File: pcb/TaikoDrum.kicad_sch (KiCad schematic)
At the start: 23 parts, among them J1 USB_B_Micro, J2 Conn_02x04_Odd_Even, U1 STM32F103C8Tx, U2 LM3940IMPX-3.3_NOPB, Y1 8Mhz

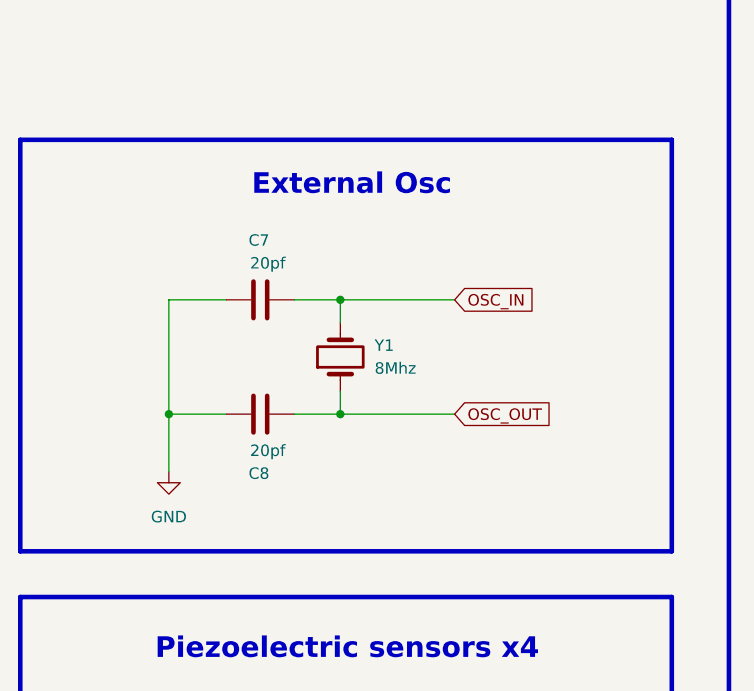
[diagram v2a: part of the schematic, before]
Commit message: Added 16M resistor for external LSE oscillator according to the STM32F103 errata recomendations.
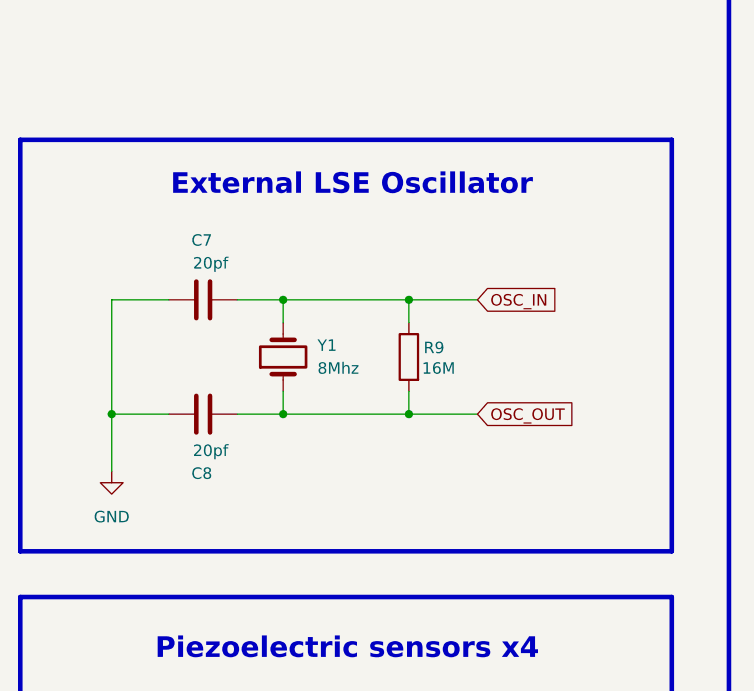
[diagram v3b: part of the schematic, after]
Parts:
- added R9: 16M, Resistor_SMD:R_0805_2012Metric, symbol Device:R
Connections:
- net OSC_IN: now also R9.1
- net OSC_OUT: now also R9.2
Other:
- note added: "External LSE Oscillator"
- note removed: "External Osc"
- moved on the sheet: C7, C8, Y1
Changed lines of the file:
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@@
 		)
 	)
-	(text "External Osc"
+	(text "External LSE Oscillator"
 		(exclude_from_sim no)
 		(at 60.96 43.18 0)
@@
 	)
 	(junction
-		(at 40.64 68.58)
+		(at 34.29 68.58)
 		(diameter 0)
 		(color 0 0 0 0)
@@
 	)
 	(junction
-		(at 59.69 55.88)
+		(at 53.34 55.88)
 		(diameter 0)
 		(color 0 0 0 0)
@@
 	)
 	(junction
-		(at 59.69 68.58)
+		(at 53.34 68.58)
 		(diameter 0)
 		(color 0 0 0 0)
@@
 	)
 	(junction
+		(at 67.31 55.88)
+		(diameter 0)
+		(color 0 0 0 0)
+	)
+	(junction
+		(at 67.31 68.58)
+		(diameter 0)
+		(color 0 0 0 0)
+	)
+	(junction
 		(at 49.53 127)
 		(diameter 0)
@@
 	(wire
 		(pts
-			(xy 40.64 68.58) (xy 40.64 55.88)
+			(xy 34.29 68.58) (xy 34.29 55.88)
 		)
 		(stroke
@@
 	(wire
 		(pts
-			(xy 54.61 68.58) (xy 59.69 68.58)
+			(xy 48.26 68.58) (xy 53.34 68.58)
+		)
+		(stroke
+			(width 0)
+			(type default)
+		)
+	)
+	(wire
+		(pts
+			(xy 53.34 55.88) (xy 67.31 55.88)
 		)
 		(stroke
@@
 	(wire
 		(pts
+			(xy 67.31 66.04) (xy 67.31 68.58)
+		)
+		(stroke
+			(width 0)
+			(type default)
+		)
+	)
+	(wire
+		(pts
 			(xy 55.88 115.57) (xy 76.2 115.57)
 		)
@@
 	(wire
 		(pts
-			(xy 40.64 55.88) (xy 46.99 55.88)
+			(xy 34.29 55.88) (xy 40.64 55.88)
 		)
 		(stroke
@@
 	(wire
 		(pts
+			(xy 67.31 55.88) (xy 67.31 58.42)
+		)
+		(stroke
+			(width 0)
+			(type default)
+		)
+	)
+	(wire
+		(pts
 			(xy 139.7 128.27) (xy 138.43 128.27)
 		)
@@
 	(wire
 		(pts
-			(xy 59.69 68.58) (xy 59.69 66.04)
+			(xy 53.34 68.58) (xy 53.34 66.04)
 		)
 		(stroke
@@
 	(wire
 		(pts
-			(xy 72.39 55.88) (xy 59.69 55.88)
+			(xy 74.93 55.88) (xy 67.31 55.88)
 		)
 		(stroke
@@
 	(wire
 		(pts
-			(xy 40.64 74.93) (xy 40.64 68.58)
+			(xy 34.29 74.93) (xy 34.29 68.58)
 		)
 		(stroke
@@
 	(wire
 		(pts
-			(xy 59.69 58.42) (xy 59.69 55.88)
+			(xy 53.34 58.42) (xy 53.34 55.88)
 		)
 		(stroke
@@
 	(wire
 		(pts
-			(xy 40.64 68.58) (xy 46.99 68.58)
+			(xy 34.29 68.58) (xy 40.64 68.58)
 		)
 		(stroke
@@
 	(wire
 		(pts
-			(xy 72.39 68.58) (xy 59.69 68.58)
+			(xy 74.93 68.58) (xy 67.31 68.58)
 		)
 		(stroke
@@
 	(wire
 		(pts
+			(xy 53.34 68.58) (xy 67.31 68.58)
+		)
+		(stroke
+			(width 0)
+			(type default)
+		)
+	)
+	(wire
+		(pts
 			(xy 57.15 107.95) (xy 80.01 107.95)
 		)
@@
 	(wire
 		(pts
-			(xy 59.69 55.88) (xy 54.61 55.88)
+			(xy 53.34 55.88) (xy 48.26 55.88)
 		)
 		(stroke
@@
 	(global_label "OSC_OUT"
 		(shape input)
-		(at 72.39 68.58 0)
+		(at 74.93 68.58 0)
 		(fields_autoplaced yes)
 		(effects
@@
 		)
 		(property "Intersheetrefs" "${INTERSHEET_REFS}"
-			(at 83.7814 68.58 0)
+			(at 86.3214 68.58 0)
 			(effects
 				(font
@@
 	(global_label "OSC_IN"
 		(shape input)
-		(at 72.39 55.88 0)
+		(at 74.93 55.88 0)
 		(fields_autoplaced yes)
 		(effects
@@
 		)
 		(property "Intersheetrefs" "${INTERSHEET_REFS}"
-			(at 82.0881 55.88 0)
+			(at 84.6281 55.88 0)
 			(effects
 				(font
@@
 	(symbol
 		(lib_id "Device:Crystal")
-		(at 59.69 62.23 90)
+		(at 53.34 62.23 90)
 		(unit 1)
 		(exclude_from_sim no)
@@
 		(fields_autoplaced yes)
 		(property "Reference" "Y1"
-			(at 63.5 60.9599 90)
+			(at 57.15 60.9599 90)
 			(effects
 				(font
@@
 		)
 		(property "Value" "8Mhz"
-			(at 63.5 63.4999 90)
+			(at 57.15 63.4999 90)
 			(effects
 				(font
@@
 		)
 		(property "Footprint" ""
-			(at 59.69 62.23 0)
+			(at 53.34 62.23 0)
 			(effects
 				(font
@@
 		)
 		(property "Datasheet" "~"
-			(at 59.69 62.23 0)
+			(at 53.34 62.23 0)
 			(effects
 				(font
@@
 		)
 		(property "Description" "Two pin crystal"
-			(at 59.69 62.23 0)
+			(at 53.34 62.23 0)
 			(effects
 				(font
@@
 	(symbol
 		(lib_id "Device:C")
-		(at 50.8 55.88 90)
+		(at 44.45 55.88 90)
 		(unit 1)
 		(exclude_from_sim no)
@@
 		(dnp no)
 		(property "Reference" "C7"
-			(at 51.816 49.276 90)
+			(at 45.466 49.276 90)
 			(effects
 				(font
@@
 		)
 		(property "Value" "20pf"
-			(at 53.594 51.816 90)
+			(at 47.244 51.816 90)
 			(effects
 				(font
@@
 		)
 		(property "Footprint" "Capacitor_SMD:C_0805_2012Metric_Pad1.18x1.45mm_HandSolder"
-			(at 54.61 54.9148 0)
+			(at 48.26 54.9148 0)
 			(effects
 				(font
@@
 		)
 		(property "Datasheet" "~"
-			(at 50.8 55.88 0)
+			(at 44.45 55.88 0)
 			(effects
 				(font
@@
 		)
 		(property "Description" "Unpolarized capacitor"
-			(at 50.8 55.88 0)
+			(at 44.45 55.88 0)
 			(effects
 				(font
@@
 	(symbol
 		(lib_id "Device:C")
-		(at 50.8 68.58 90)
+		(at 44.45 68.58 90)
 		(mirror x)
 		(unit 1)
@@
 		(dnp no)
 		(property "Reference" "C8"
-			(at 51.816 75.184 90)
+			(at 45.466 75.184 90)
 			(effects
 				(font
@@
 		)
 		(property "Value" "20pf"
-			(at 53.594 72.644 90)
+			(at 47.244 72.644 90)
 			(effects
 				(font
@@
 		)
 		(property "Footprint" "Capacitor_SMD:C_0805_2012Metric_Pad1.18x1.45mm_HandSolder"
-			(at 54.61 69.5452 0)
+			(at 48.26 69.5452 0)
 			(effects
 				(font
@@
 		)
 		(property "Datasheet" "~"
-			(at 50.8 68.58 0)
+			(at 44.45 68.58 0)
 			(effects
 				(font
@@
 		)
 		(property "Description" "Unpolarized capacitor"
-			(at 50.8 68.58 0)
+			(at 44.45 68.58 0)
 			(effects
 				(font
@@
 	)
 	(symbol
+		(lib_id "Device:R")
+		(at 67.31 62.23 0)
+		(mirror y)
+		(unit 1)
+		(exclude_from_sim no)
+		(in_bom yes)
+		(on_board yes)
+		(dnp no)
+		(property "Reference" "R9"
+			(at 70.104 61.214 0)
+			(effects
+				(font
+					(size 1.27 1.27)
+				)
+			)
+		)
+		(property "Value" "16M"
+			(at 70.612 63.5 0)
+			(effects
+				(font
+					(size 1.27 1.27)
+				)
+			)
+		)
+		(property "Footprint" "Resistor_SMD:R_0805_2012Metric"
+			(at 69.088 62.23 90)
+			(effects
+				(font
+					(size 1.27 1.27)
+				)
+				(hide yes)
+			)
+		)
+		(property "Datasheet" "~"
+			(at 67.31 62.23 0)
+			(effects
+				(font
+					(size 1.27 1.27)
+				)
+				(hide yes)
+			)
+		)
+		(property "Description" "Resistor"
+			(at 67.31 62.23 0)
+			(effects
+				(font
+					(size 1.27 1.27)
+				)
+				(hide yes)
+			)
+		)
+		(pin "1"
+		)
+		(pin "2"
+		)
+		(instances
+			(project "TaikoDrum"
+				(path "/ee4ada02-05a0-4e49-92f9-f61a706c8588"
+					(reference "R9")
+					(unit 1)
+				)
+			)
+		)
+	)
+	(symbol
 		(lib_id "Switch:SW_SPST")
 		(at 36.83 172.72 90)
@@
 	(symbol
 		(lib_id "power:GND")
-		(at 40.64 74.93 0)
+		(at 34.29 74.93 0)
 		(unit 1)
 		(exclude_from_sim no)
@@
 		(fields_autoplaced yes)
 		(property "Reference" "#PWR019"
-			(at 40.64 81.28 0)
+			(at 34.29 81.28 0)
 			(effects
 				(font
@@
 		)
 		(property "Value" "GND"
-			(at 40.64 80.01 0)
+			(at 34.29 80.01 0)
 			(effects
 				(font
@@
 		)
 		(property "Footprint" ""
-			(at 40.64 74.93 0)
+			(at 34.29 74.93 0)
 			(effects
 				(font
@@
 		)
 		(property "Datasheet" ""
-			(at 40.64 74.93 0)
+			(at 34.29 74.93 0)
 			(effects
 				(font
@@
 		)
 		(property "Description" "Power symbol creates a global label with name \"GND\" , ground"
-			(at 40.64 74.93 0)
+			(at 34.29 74.93 0)
 			(effects
 				(font

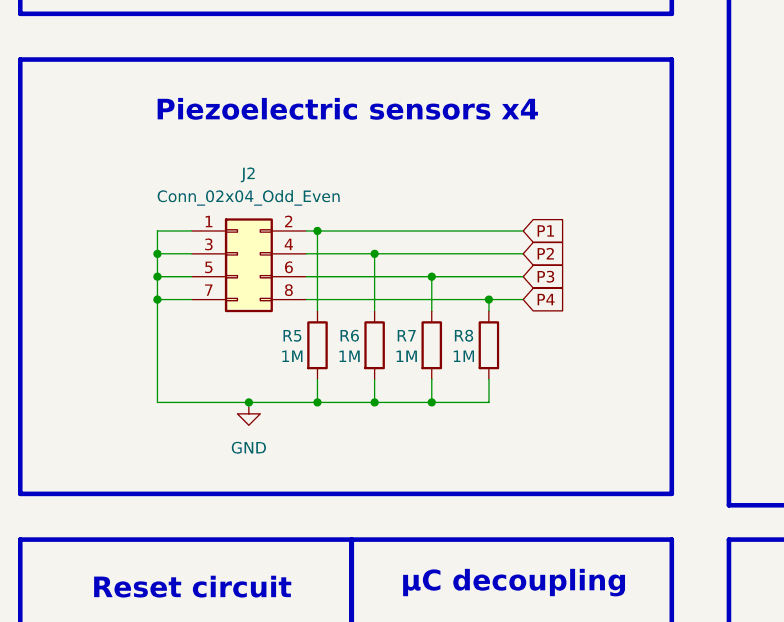
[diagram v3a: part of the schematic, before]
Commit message: Used an additional voltage divider to not loose any energy from the piezo signal.
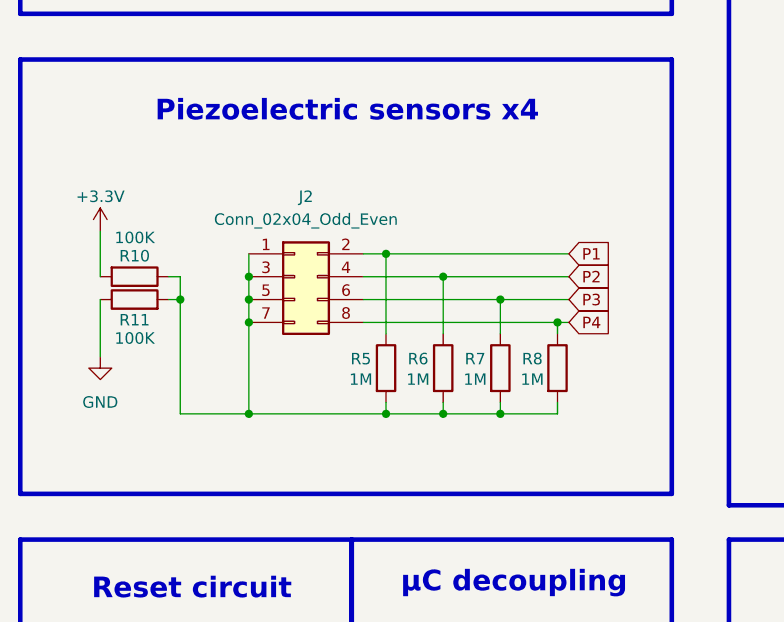
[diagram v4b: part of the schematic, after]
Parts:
- added R10, R11: 100K, Resistor_SMD:R_0805_2012Metric, symbol Device:R
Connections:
- net +3.3V: now also R10.2
- net GND: now also R11.1; no longer J2.1 (Pin_1), J2.3 (Pin_3), J2.5 (Pin_5), J2.7 (Pin_7), R5.2, R6.2, R7.2, R8.2
- new net: J2.1 (Pin_1), J2.3 (Pin_3), J2.5 (Pin_5), J2.7 (Pin_7), R10.1, R11.2, R5.2, R6.2, R7.2, R8.2
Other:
- moved on the sheet: J2, R5, R6, R7, R8

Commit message: Updated PCB schematic.
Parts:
- added D1: PWR, LED_THT:LED_D3.0mm, symbol Device:LED
- added H1, H2, H3, H4: MountingHole, MountingHole:MountingHole_2.2mm_M2, symbol Mechanical:MountingHole
- added R12: 1K, Resistor_THT:R_Axial_DIN0204_L3.6mm_D1.6mm_P2.54mm_Vertical, symbol Device:R
- C3, C4, C5, C6, C7, C8: footprint Capacitor_SMD:C_0805_2012Metric_Pad1.18x1.45mm_HandSolder -> Capacitor_THT:C_Radial_D5.0mm_H5.0mm_P2.00mm
- R1, R10, R11, R2, R3, R4, R5, R6, R7, R8, R9: footprint Resistor_SMD:R_0805_2012Metric -> Resistor_THT:R_Axial_DIN0204_L3.6mm_D1.6mm_P2.54mm_Vertical
- Y1: footprint (none) -> Crystal:Crystal_HC52-U_Vertical
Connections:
- net +3.3V: now also R12.2
- net GND: now also D1.1 (K)
- new net: D1.2 (A), R12.1
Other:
- note added: "Miscs"
- note removed: "Reset circuit"
- note removed: "µC decoupling"
- moved on the sheet: C1, C2, C3, C4, C5, C6, C7, C8, J1, J2, R1, R10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

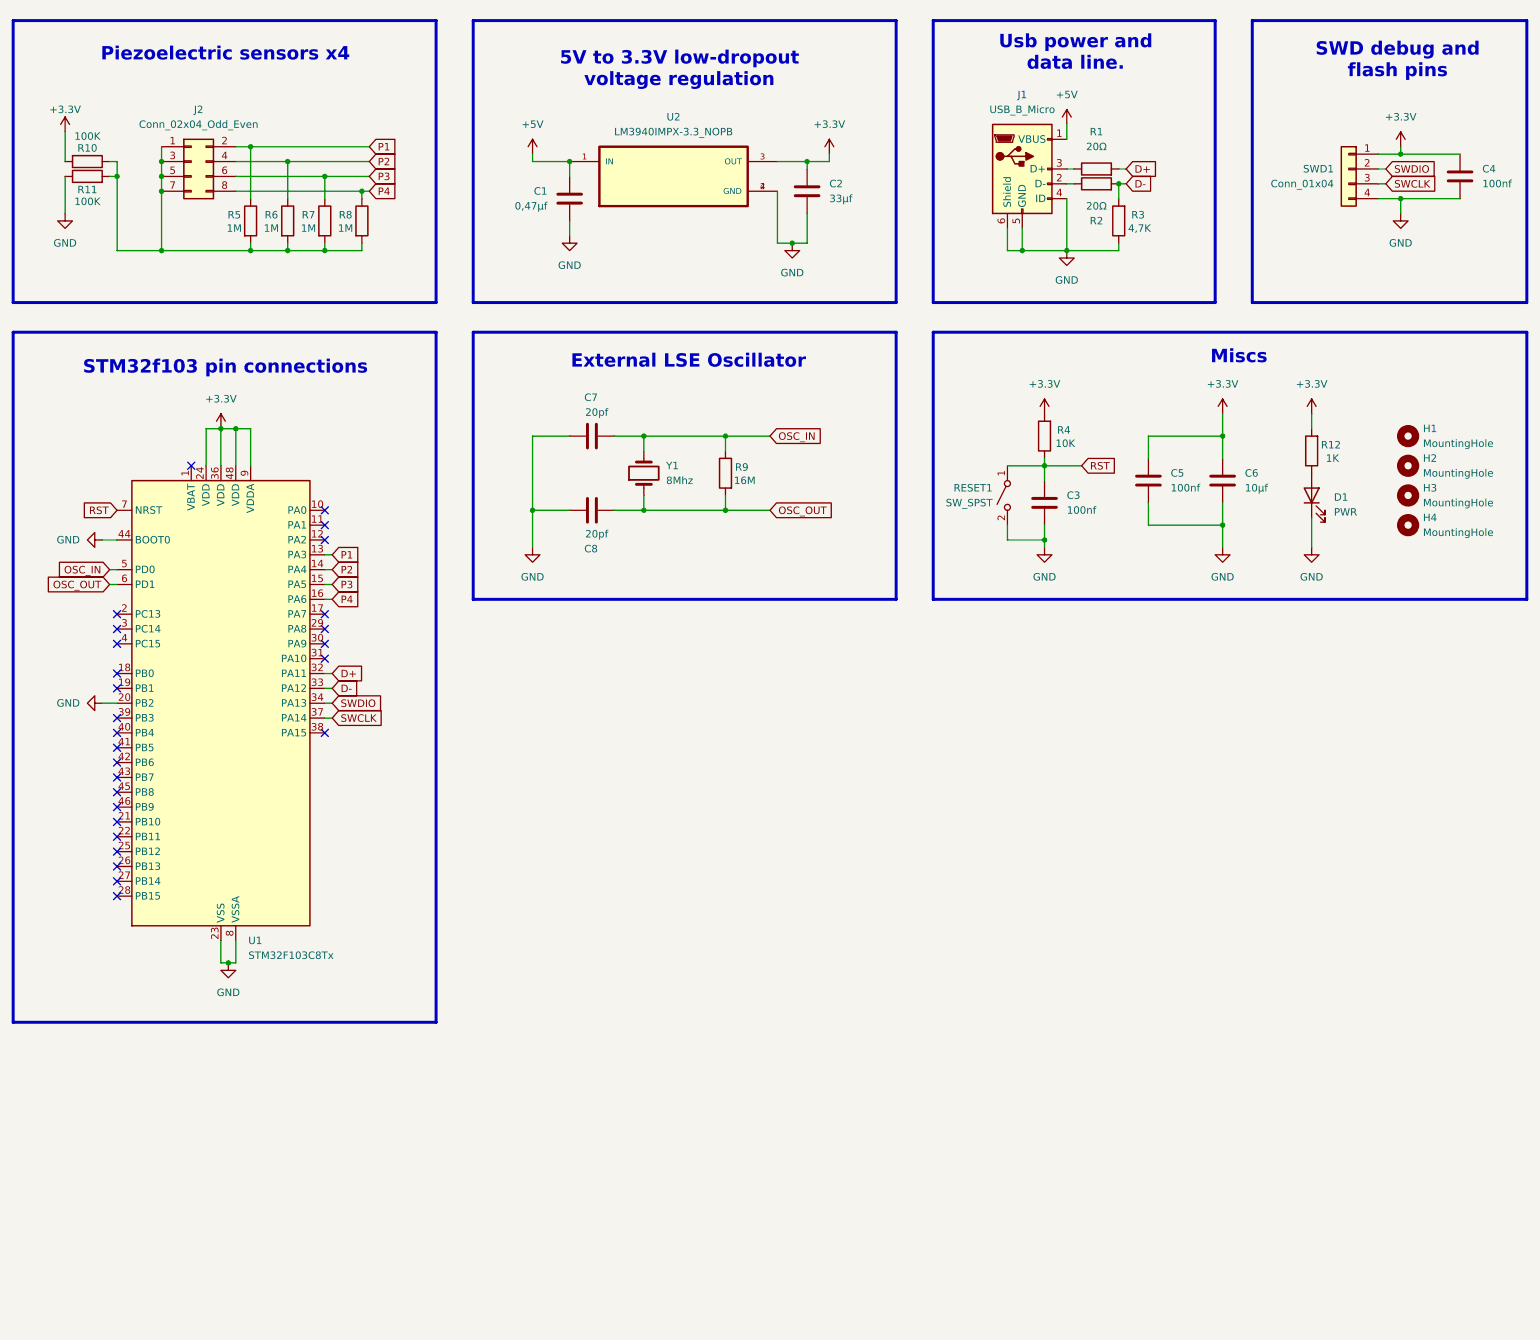
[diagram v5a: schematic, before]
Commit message: Better LM358 based op-amp buffering for piezo voltage dividers.
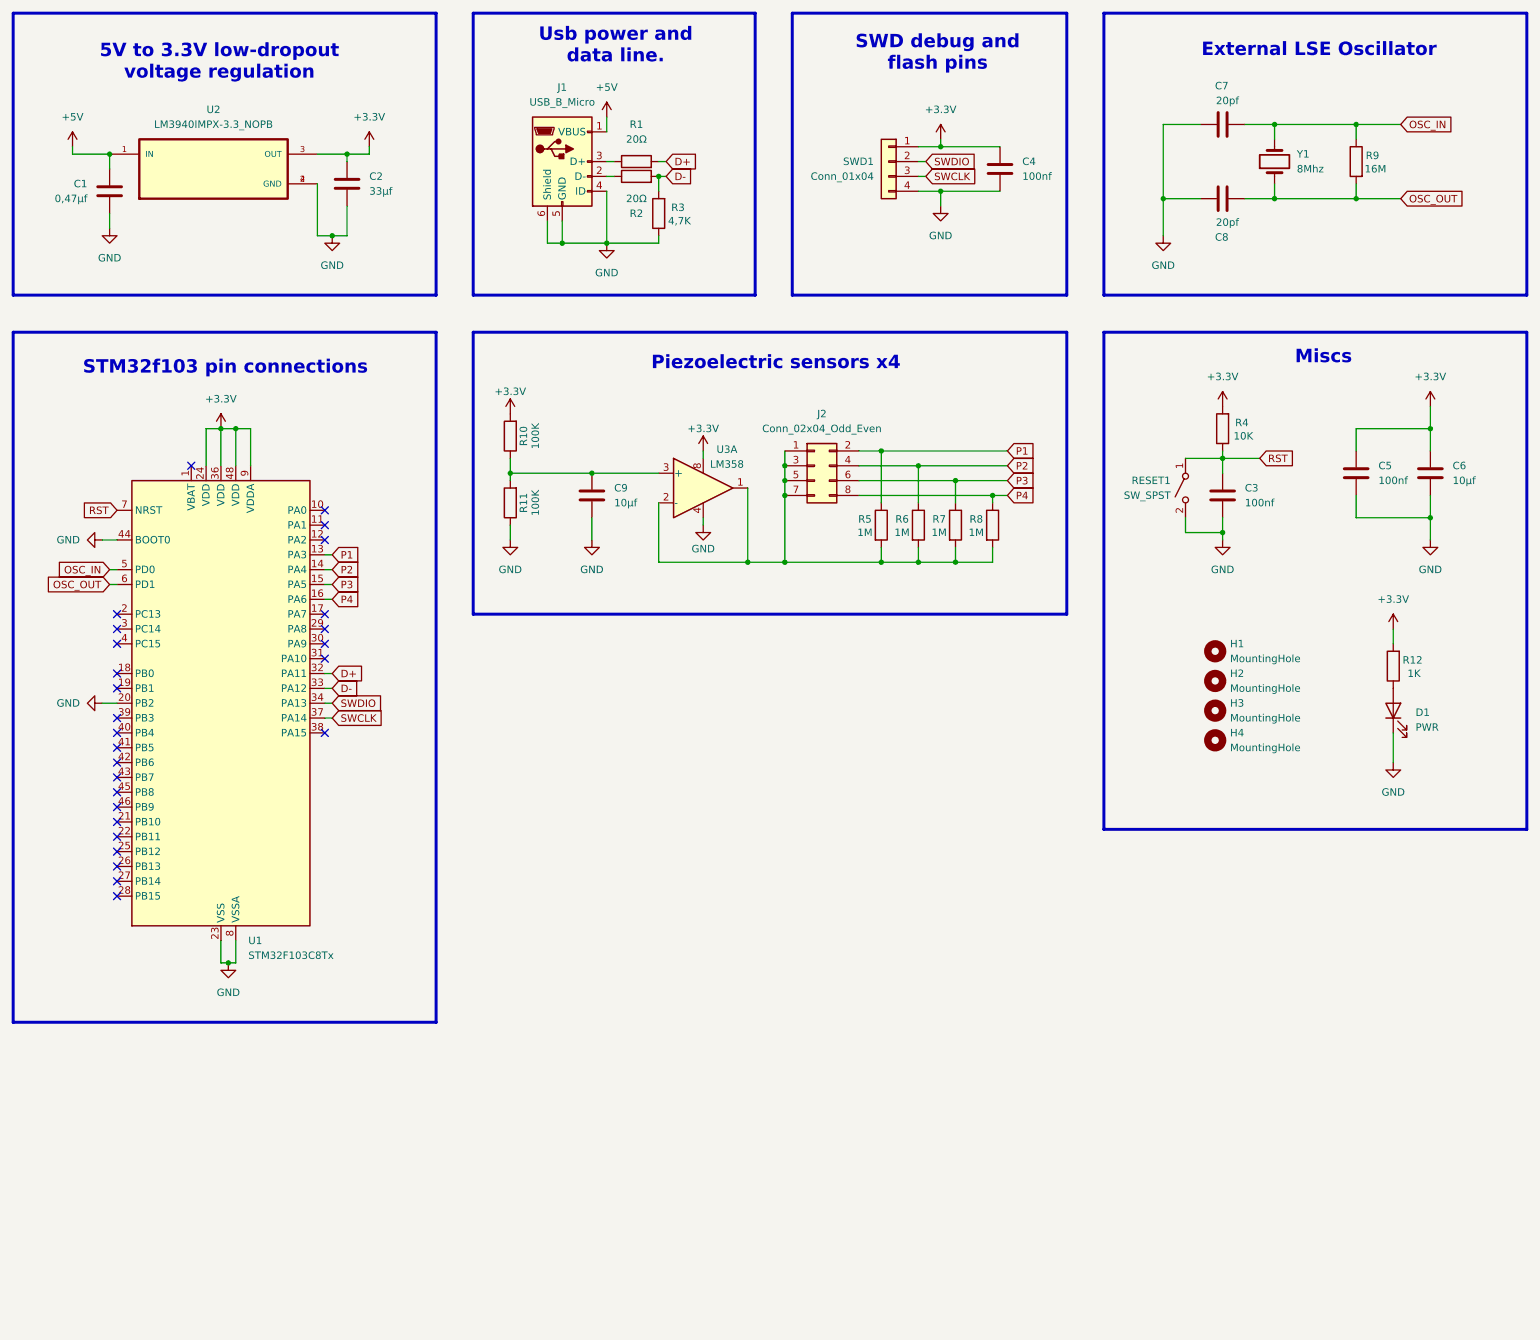
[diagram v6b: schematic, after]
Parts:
- added C9: 10µf, Capacitor_SMD:C_0805_2012Metric_Pad1.18x1.45mm_HandSolder, symbol Device:C
- added U3: LM358, Package_DIP:DIP-8_W7.62mm, symbol Amplifier_Operational:LM358
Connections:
- net +3.3V: now also U3.8
- net GND: now also C9.2, U3.4
- net at J2.1 (Pin_1), J2.3 (Pin_3), J2.5 (Pin_5)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: now also U3.1, U3.2 (-); no longer R10.1, R11.2
- new net: C9.1, R10.1, R11.2, U3.3 (+)
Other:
- moved on the sheet: C1, C2, C3, C4, C5, C6, C7, C8, D1, H1, H2, H3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
